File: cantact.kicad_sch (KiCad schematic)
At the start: 37 parts, among them P1 USB, P2 SWD, P3 DB9, U1 STM32F042C6T6, U2 AAT3221, U3 MCP2551-I/SN, X1 16 MHz

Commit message: feat(hw):  schematic & pcb updated
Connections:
- net CAN_RX: now also U3.4 (RXD); no longer U3.1 (TXD)
- net CAN_TX: now also U3.1 (TXD); no longer U3.4 (RXD)
- net DB9_1: now also P3.1; no longer P3.5
- net DB9_2: now also P3.2; no longer P3.4
- net DB9_5: now also P3.5; no longer P3.1
- net DB9_7: now also P3.7; no longer P3.8
- net at D1.1 (K): now also R2.2; no longer U1.18 (PB0)
- net at D2.1 (K): now also R3.2; no longer U1.19 (PB1)
- net LED_GREEN: now reaches D1.2 (A)
- net LED_GREEN: now also U1.18 (PB0); no longer R2.2
- net LED_RED: now reaches D2.2 (A)
- net LED_RED: now also U1.19 (PB1); no longer R3.2
- no-connect marks 0 -> 34
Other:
- note added: "CAN"
- note added: "CAN Output"
- note added: "LEDs"
- note added: "Power Supply"
- note added: "STM32"
- note added: "SWD"
- moved on the sheet: C1, C10, C11, C12, C13, C14, C15, C16, C2, C3, C4, C5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

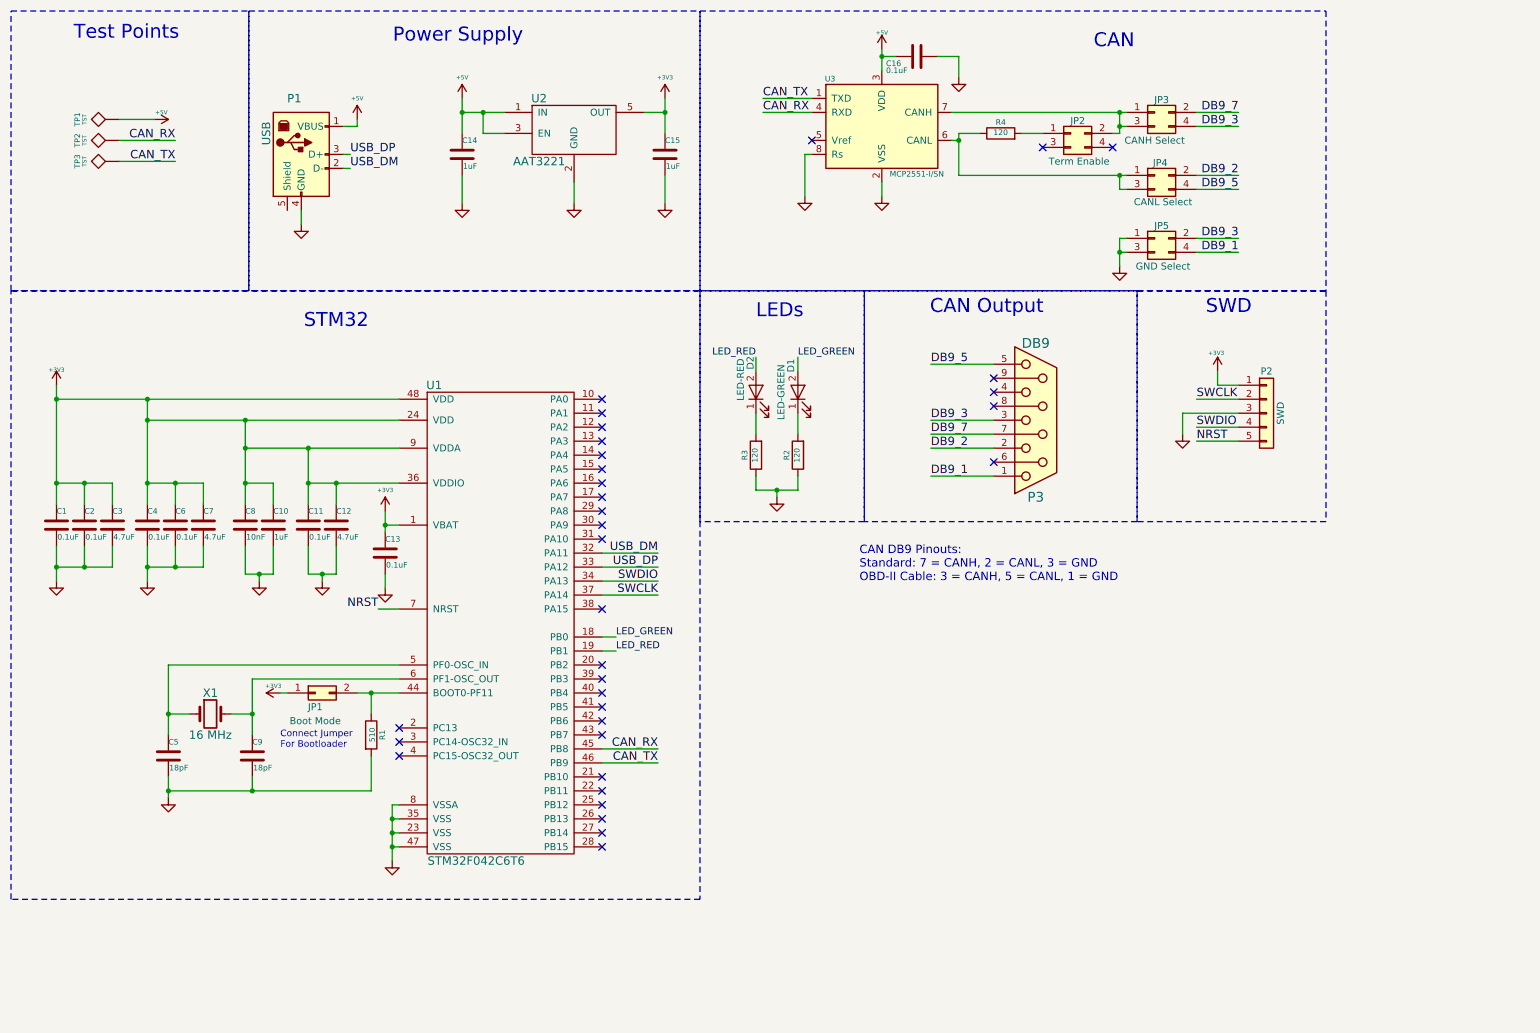
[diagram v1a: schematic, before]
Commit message: feat: replace USB & RJ45 ports
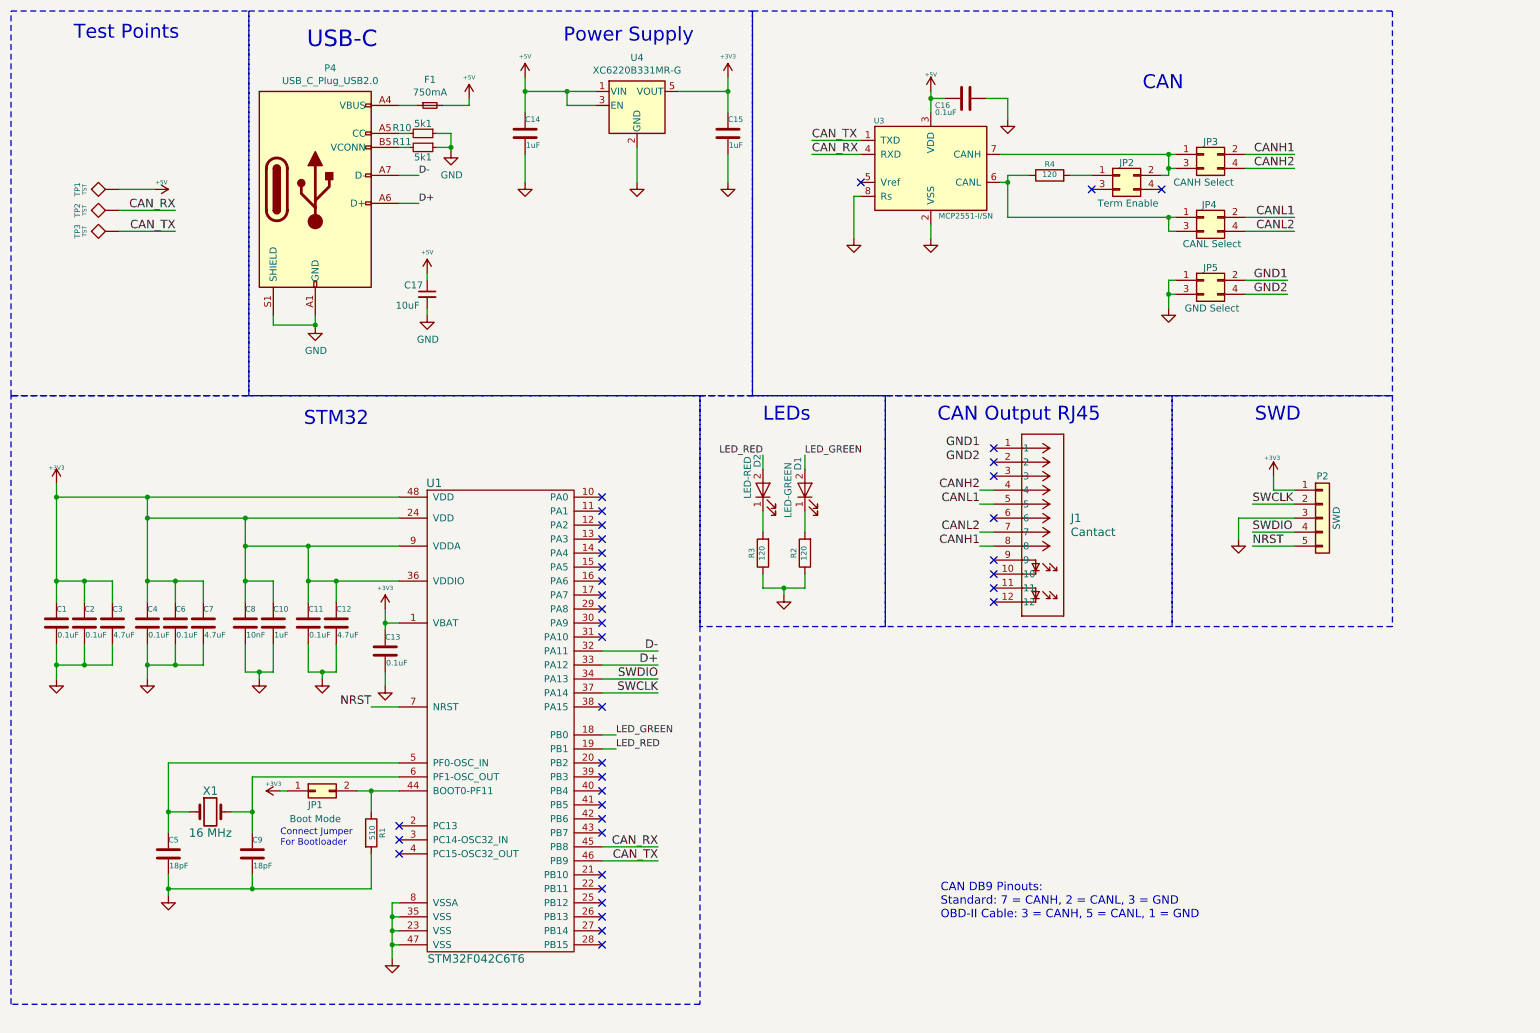
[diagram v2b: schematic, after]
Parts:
- removed P1: USB, Connect:USB_B, symbol cantact-rescue:USB_B
- removed P3: DB9, Connect:DB9MC, symbol cantact-rescue:DB9_Female
- removed U2: AAT3221, SMD_Packages:SOT-23-5, symbol cantact:AAT3221
- added C17: 10uF, Capacitor_SMD:C_0603_1608Metric, symbol Device:C_Small
- added F1: 750mA, Fuse:Fuse_0603_1608Metric, symbol Device:Fuse_Small
- added J1: Cantact, footprints:CONN12_R-RJ45_CKM, symbol cantact_ec:RJ45_Male
- added P4: USB_C_Plug_USB2.0, C393939, symbol HunterCat-NFC-rescue:USB_C_Plug_USB2.0-Connector
- added R10, R11: 5k1, Resistor_SMD:R_0603_1608Metric, symbol Device:R_Small
- added U4: XC6220B331MR-G, Package_TO_SOT_SMD:SOT-23-5, symbol HunterCat-NFC-rescue:AP2112K-3.3-Regulator_Linear
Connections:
- net +3V3: now also U4.5 (VOUT)
- net +5V: now also C17.1, F1.2, U4.1 (VIN), U4.3 (EN)
- net GND: now also C17.2, P4.A1 (GND), P4.A12 (GND), P4.B1 (GND), P4.B12 (GND), P4.S1 (SHIELD), R10.1, R11.1, U4.2 (GND)
- net DB9_1 renamed GND2
- net DB9_2 renamed CANL1
- net CANL1: now also J1.5
- net DB9_3 renamed CANH2
- net CANH2: now also J1.4; no longer JP5.2 (Pin_2)
- net DB9_5 renamed CANL2
- net CANL2: now also J1.7
- net DB9_7 renamed CANH1
- net CANH1: now also J1.8
- net USB_DM renamed D-
- net D-: now also P4.A7 (D-)
- net USB_DP renamed D+
- net D+: now also P4.A6 (D+)
- new net: F1.1, P4.A4 (VBUS), P4.A9 (VBUS), P4.B4 (VBUS), P4.B9 (VBUS)
- new net: P4.A5 (CC), R10.2
- new net: P4.B5 (VCONN), R11.2
- new net GND1: JP5.2 (Pin_2)
- no-connect marks 34 -> 38
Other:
- note added: "CAN Output RJ45"
- note added: "USB-C"
- note removed: "CAN Output"
- moved on the sheet: C1, C10, C11, C12, C13, C14, C15, C16, C2, C3, C4, C5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

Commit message: refactor(hw): PCB routing
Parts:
- removed D1: LED-GREEN, SMD_Packages:SMD-0603, symbol cantact-rescue:LED
- removed D2: LED-RED, SMD_Packages:SMD-0603, symbol cantact-rescue:LED
- removed X1: 16 MHz, Crystals:Crystal_HC49-SD_SMD, symbol cantact-rescue:Crystal
- added Y1: 16 Mhz, Crystal:Crystal_SMD_2016-4Pin_2.0x1.6mm, symbol Device:Crystal_GND24
- C1, C11, C13, C16, C2, C4, C6: LCSC# (none) -> C478888
- C10, C14, C15: LCSC# (none) -> C15849
- C12, C3, C7: footprint Capacitors_SMD:C_0603 -> Capacitor_SMD:C_0805_2012Metric_Pad1.18x1.45mm_HandSolder; LCSC# (none) -> C98192; manf# (none) -> CL21A475KBQNNNE
- C5, C9: LCSC# (none) -> C1647
- C8: LCSC# (none) -> C1589
- J1: LCSC# (none) -> C386757; manf# (none) -> R-RJ45R08P-C000
- JP1: LCSC# (none) -> C7501580; manf# (none) -> PH2.54-01-02PZD; now not fitted
- JP2, JP3, JP4, JP5: LCSC# (none) -> C780055; manf# (none) -> X6521WVS-2x02H-C60D74
- P2: LCSC# (none) -> C7501583; manf# (none) -> PH2.54-01-05PZD; now not fitted
- R1: footprint SMD_Packages:SMD-0603 -> Resistor_SMD:R_0603_1608Metric_Pad0.98x0.95mm_HandSolder; LCSC# (none) -> C217366; manf# (none) -> CR-03JL7--510R
- R2, R3: footprint SMD_Packages:SMD-0603 -> Resistor_SMD:R_0603_1608Metric_Pad0.98x0.95mm_HandSolder; LCSC# (none) -> C2828631
- R4: footprint SMD_Packages:SMD-0603 -> Resistor_SMD:R_0603_1608Metric_Pad0.98x0.95mm_HandSolder; LCSC# (none) -> C2828631; manf# (none) -> AR03BTCX1200
- TP1, TP2, TP3: now not fitted
- U1: LCSC# (none) -> C88447; manf# (none) -> STM32F042C6T6
- U3: LCSC# (none) -> C7376; manf# (none) -> MCP2551-I/SN
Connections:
- net CANH1: now also J1.4, JP3.4 (Pin_4); no longer J1.8, JP3.2 (Pin_2)
- net CANH2: now also JP3.2 (Pin_2); no longer J1.4, JP3.4 (Pin_4)
- net CANL2: no longer J1.7
- net GND: now also R2.2, R3.2, Y1.2, Y1.4; no longer R2.1, R3.1
- net GND1: now also J1.7
- net LED_GREEN: now also J1.11
- net LED_RED: now also J1.9
- net at C5.1, U1.5 (PF0-OSC_IN): now also Y1.1
- net at C9.1, U1.6 (PF1-OSC_OUT): now also Y1.3
- net at J1.10: now also R3.1
- net at J1.12: now also R2.1
- no-connect marks 38 -> 35
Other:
- note removed: "LEDs"
- moved on the sheet: R2, R3

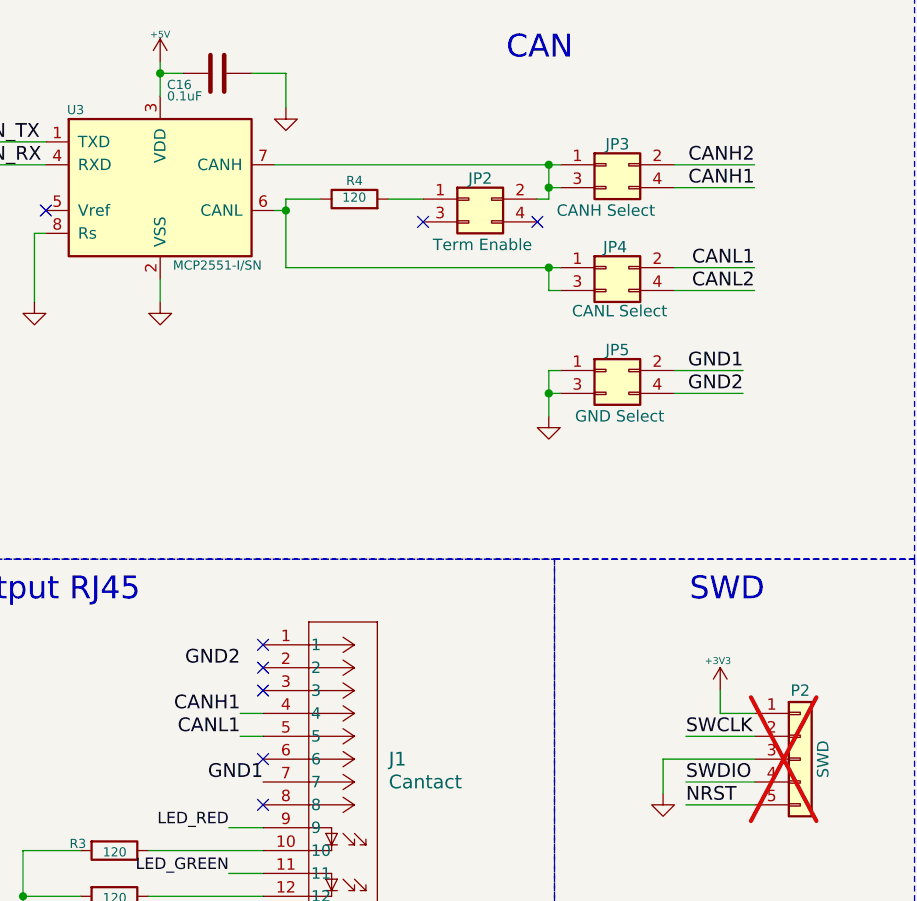
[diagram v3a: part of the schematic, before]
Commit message: feat(hw): move differential pair of CANH and CANL
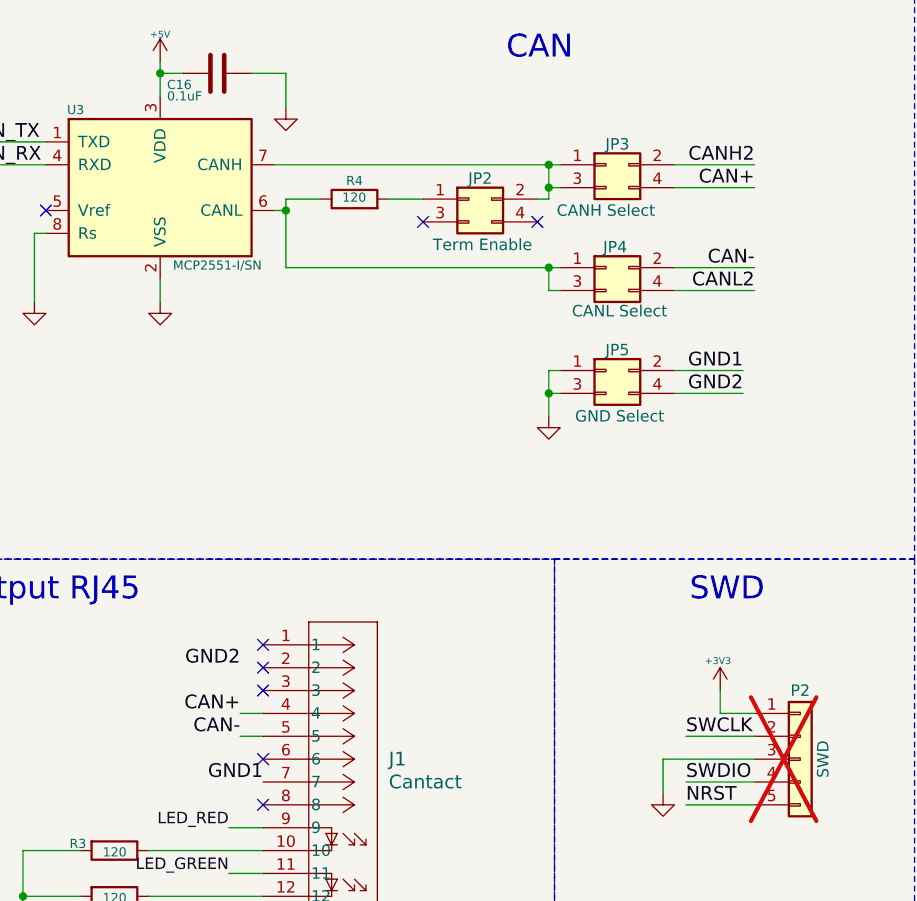
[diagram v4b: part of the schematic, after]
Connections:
- net CANH1 renamed CAN+
- net CANL1 renamed CAN-
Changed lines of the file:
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@@
 		)
 	)
-	(label "CANH1"
+	(label "CAN+"
 		(at 187.96 99.06 180)
 		(effects
@@
 		)
 	)
-	(label "CANH1"
+	(label "CAN+"
 		(at 245.11 40.64 180)
 		(effects
@@
 		)
 	)
-	(label "CANL1"
+	(label "CAN-"
 		(at 187.96 101.6 180)
 		(effects
@@
 		)
 	)
-	(label "CANL1"
+	(label "CAN-"
 		(at 245.11 49.53 180)
 		(effects

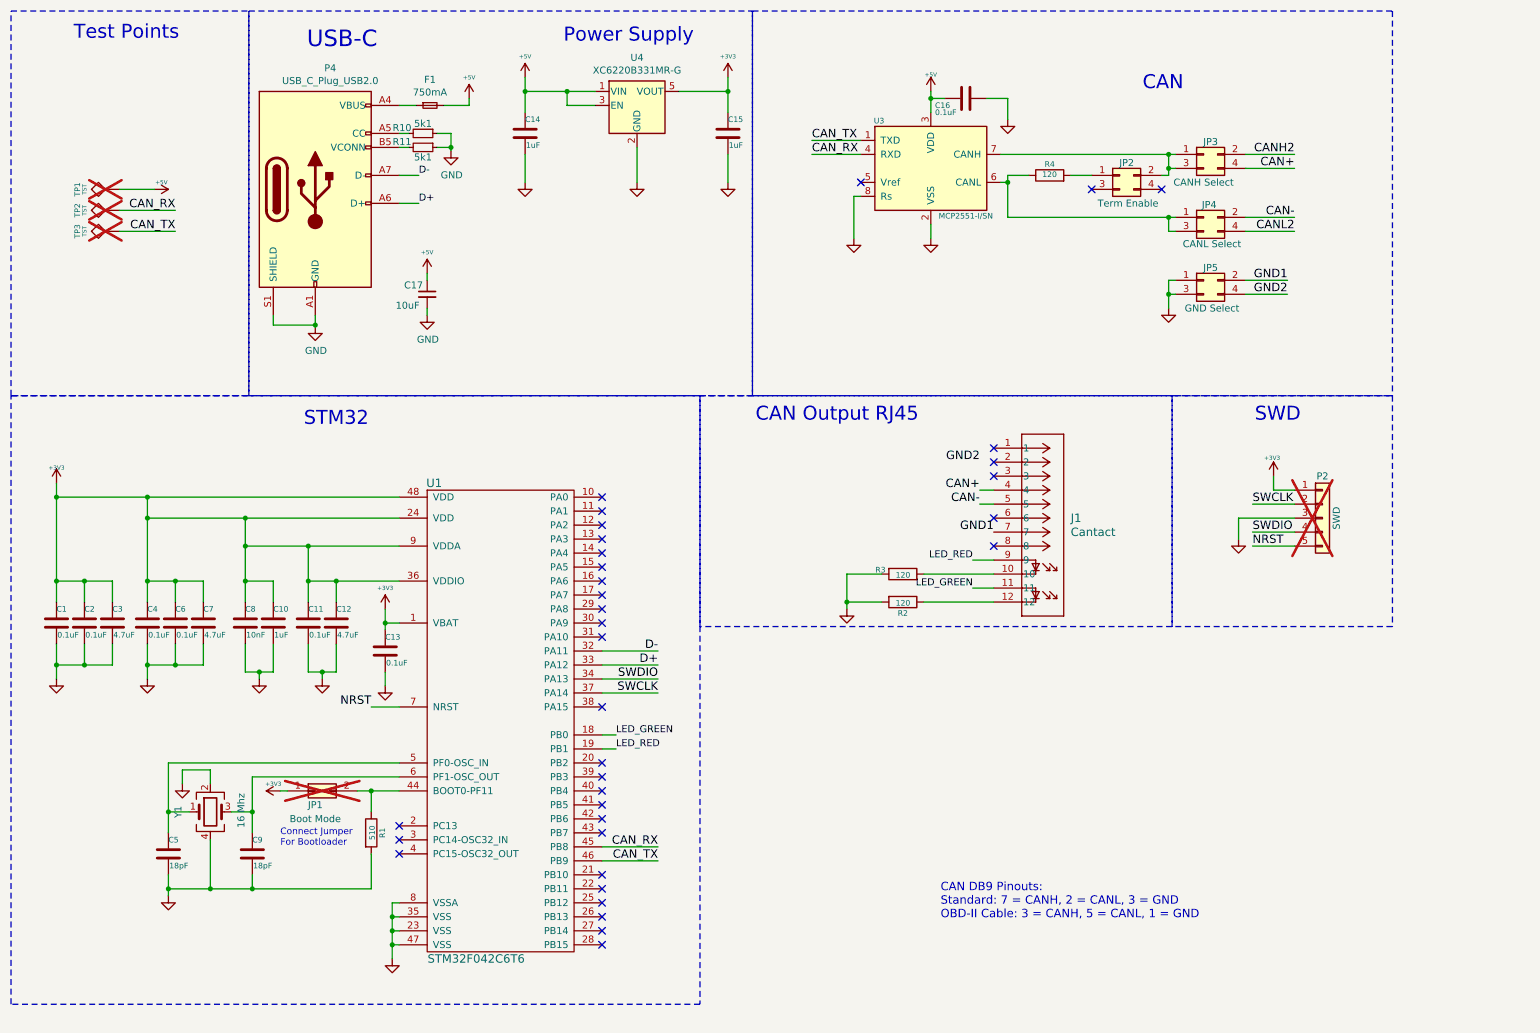
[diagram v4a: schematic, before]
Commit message: Fix: CANbus routing and added 3D models
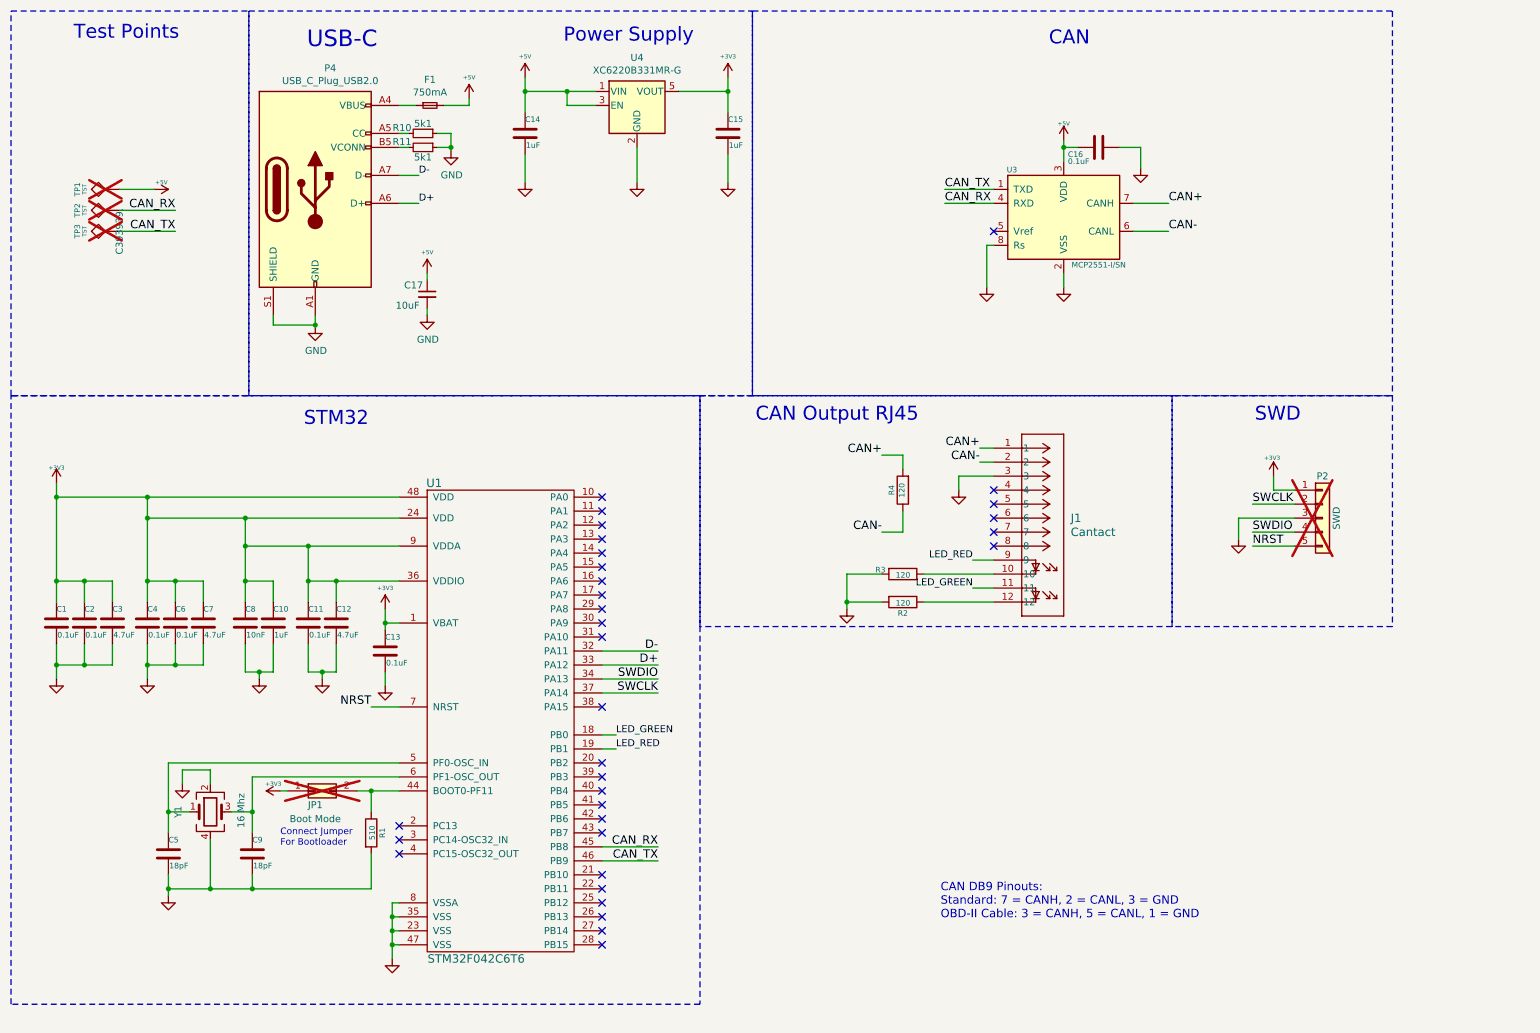
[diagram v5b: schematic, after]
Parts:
- removed JP2: Term Enable, cantact:0015912040, symbol cantact-rescue:Conn_02x02_Odd_Even
- removed JP3: CANH Select, cantact:0015912040, symbol cantact-rescue:Conn_02x02_Odd_Even
- removed JP4: CANL Select, cantact:0015912040, symbol cantact-rescue:Conn_02x02_Odd_Even
- removed JP5: GND Select, cantact:0015912040, symbol cantact-rescue:Conn_02x02_Odd_Even
- TP3: LCSC# (none) -> C393939.
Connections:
- net CAN+: now also J1.1, R4.2, U3.7 (CANH); no longer J1.4
- net CAN-: now also J1.2, R4.1, U3.6 (CANL); no longer J1.5
- net GND: now also J1.3
- net GND1: no longer names the net of J1.7
- no-connect marks 35 -> 33
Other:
- moved on the sheet: C16, R4, U3
